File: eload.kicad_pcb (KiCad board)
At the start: 2 copper layers, 78.7 x 99.1 mm, 64 parts, among them J1 Device Power, J2 Input, J3 JST Header, J4 SWD Header, J6 JST Header, J7 Conn_02x06_Odd_Even, K1 G5Q-1, Q1 TIP122, Q2 HL 40N05, Q3 DTC043Z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

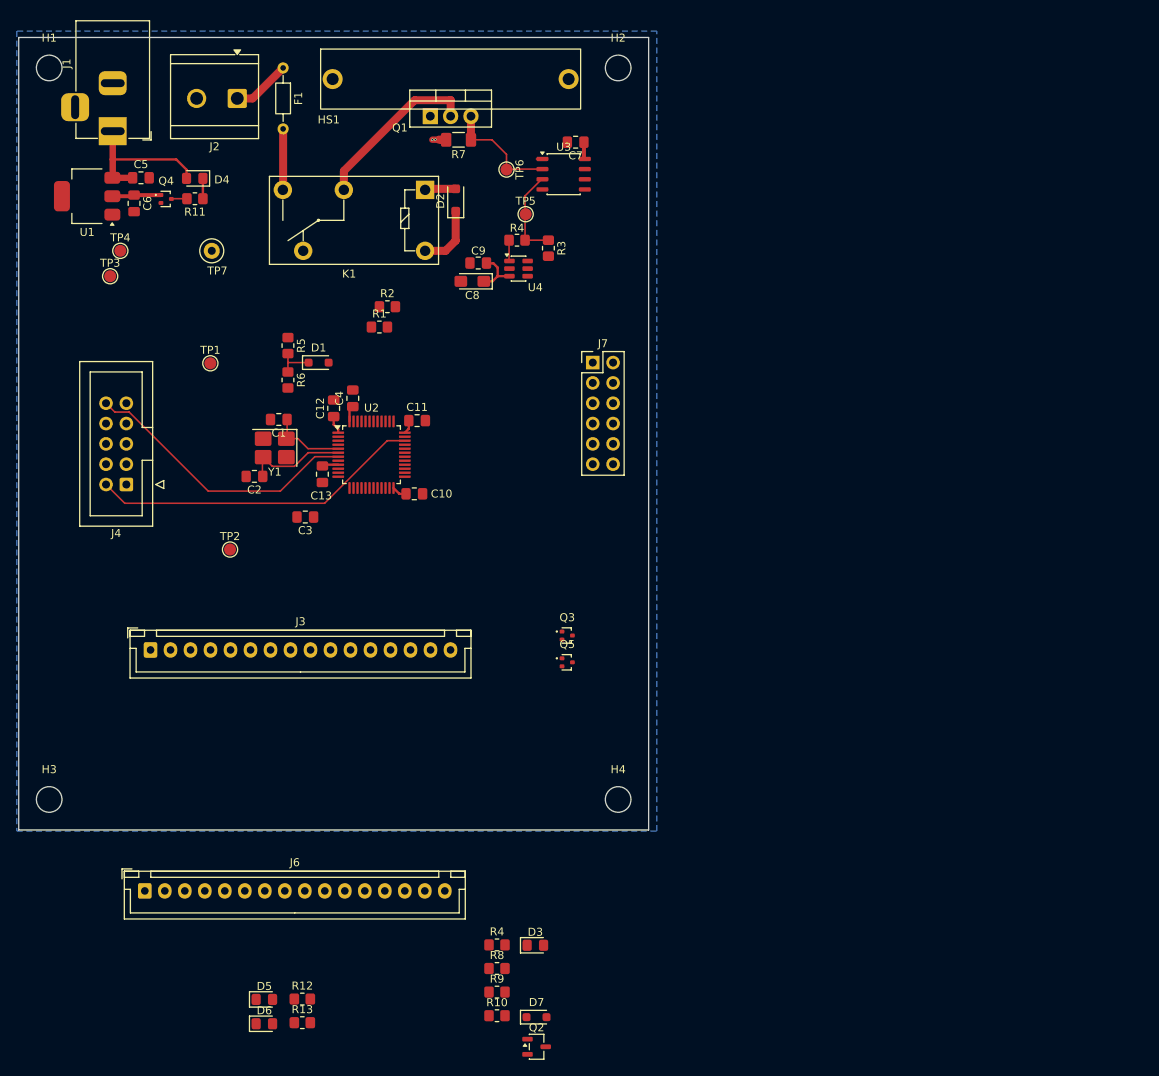
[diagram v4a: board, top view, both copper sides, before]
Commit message: PCB routing and cleanup
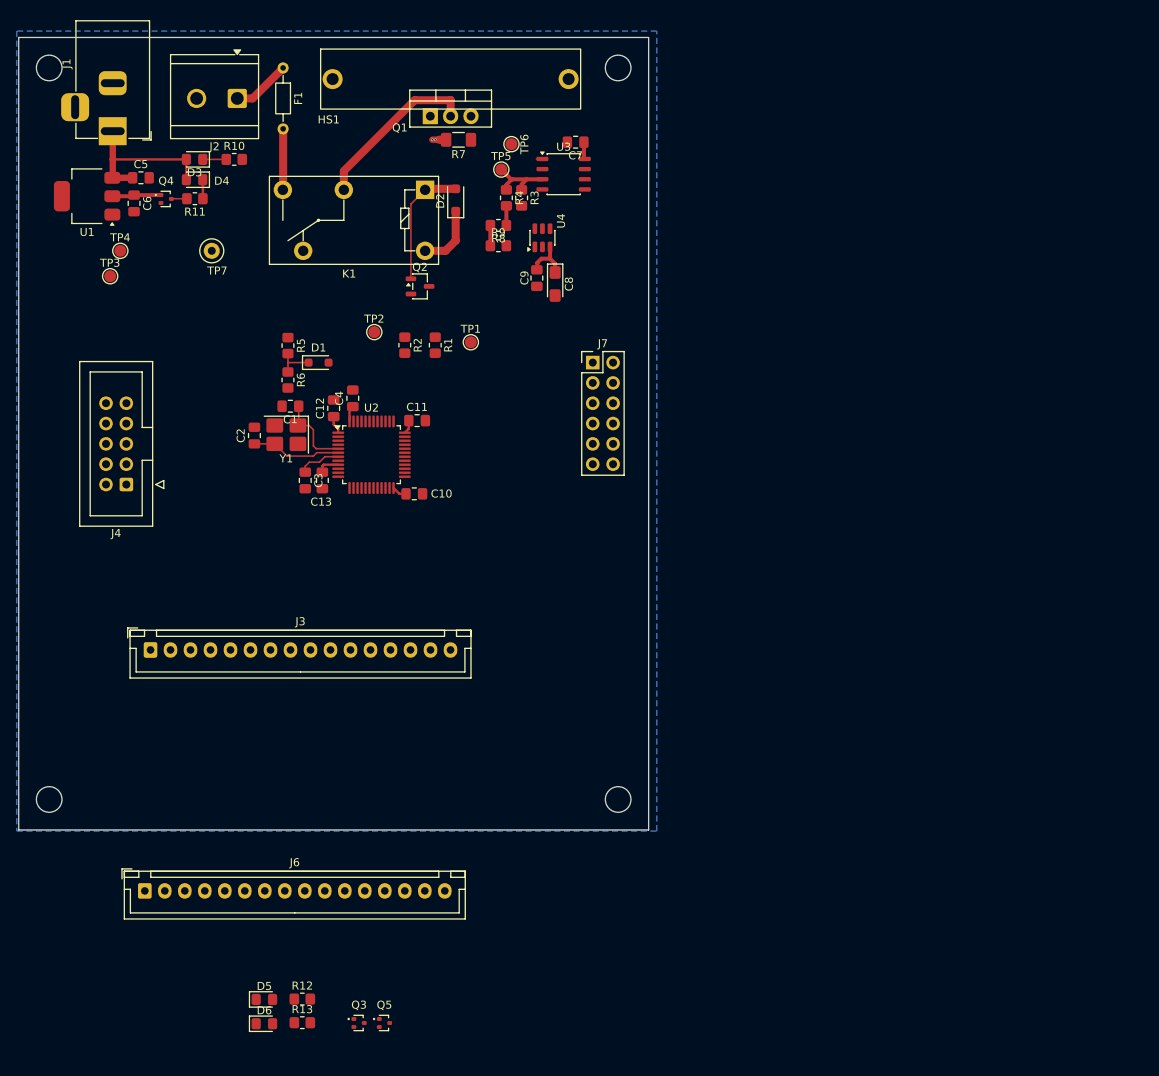
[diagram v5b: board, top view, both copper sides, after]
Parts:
- removed D7: BZT52C3V3S, Diode_SMD:D_SOD-323_HandSoldering
- removed the R4 at (77.5, 76.1)
- moved R10 112.0 mm to (42.2, 66.0)
- moved D3 107.1 mm to (37.2, 66.0), turned to 180 degrees
- moved Q2 96.2 mm to (65.4, 81.9)
- moved R4 93.4 mm to (76.2, 70.8), turned to -90 degrees
- moved R9 93.3 mm to (75.2, 76.8)
- moved R8 92.9 mm to (75.2, 74.3), turned to 180 degrees
- moved Q3 55.0 mm to (57.8, 174.0)
- moved Q5 50.5 mm to (61.0, 174.0)
- moved TP1 32.7 mm to (71.8, 88.9)
- moved TP2 32.6 mm to (59.7, 87.6)
- moved C8 10.4 mm to (82.3, 81.6), turned to -90 degrees
- moved C9 7.57 mm to (80.0, 80.9), turned to -90 degrees
- moved R1 7.34 mm to (67.3, 89.3), turned to -90 degrees
- moved R3 7.12 mm to (78.1, 70.8)
- moved TP5 6.35 mm to (75.6, 67.3)
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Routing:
- net /SWDIO: track 41.6 -> 0.00 mm
- net /~{RESET}: track 35.4 -> 5.36 mm
- net /VCC_sense: track 14.6 -> 0.00 mm
- net Net-(D2-A): track 3.88 -> 15.7 mm
- net Net-(D3-K): track 0.00 -> 2.94 mm
- net /Vctrl: track 11.5 -> 8.84 mm
- net Net-(U4-VOUT): track 2.62 -> 0.00 mm
- net Net-(R8-Pad2): track 0.00 -> 2.54 mm
- net Net-(R4-Pad2): track 0.00 -> 2.45 mm
- net /OSC2: track 13.0 -> 11.4 mm
- net +5V: track 29.4 -> 30.3 mm
- net +3.3V: track 22.2 -> 23.0 mm

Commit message: PCB routing
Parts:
- TP1: footprint TestPoint:TestPoint_Pad_D1.5mm -> TestPoint:TestPoint_Loop_D1.80mm_Drill1.0mm_Beaded
- moved R10 9.21 mm to (33.0, 67.0)
- moved C5 0.98 mm to (30.5, 69.3)
- moved C6 0.98 mm to (29.7, 72.5)
- moved D3 0.98 mm to (37.2, 67.0)
- moved D4 0.98 mm to (37.2, 69.6)
- moved Q4 0.98 mm to (33.7, 72.0)
- moved R11 0.98 mm to (37.3, 71.9)
- moved U1 0.98 mm to (23.8, 71.6)
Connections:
- D3 pad 1: Net-(D3-K) -> GND
- D3 pad 2: +5V -> Net-(D3-A)
- R10 pad 1: Net-(D3-K) -> +5V
- R10 pad 2: GND -> Net-(D3-A)
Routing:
- net Net-(D3-K): track 2.94 -> 0.00 mm
- net Net-(D3-A): track 0.00 -> 1.77 mm
- net +5V: track 30.3 -> 28.8 mm
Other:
- board text added: "3V3"
- board text added: "5V"

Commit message: Transistor updated to MOSFET
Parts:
- Q1: value TIP122 -> RFP30N06LE-VB
- moved Q1 0.32 mm to (66.7, 61.0)
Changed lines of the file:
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@@
 	(net 18 "/SWCLK")
 	(net 19 "/SWDIO")
-	(net 20 "Net-(Q1-B)")
+	(net 20 "Net-(Q1-G)")
 	(net 21 "/VCC_sense")
 	(net 22 "VCC")
@@
 		)
 	)
+	(footprint "Package_TO_SOT_THT:TO-220-3_Vertical"
+		(layer "F.Cu")
+		(at 66.69 60.96)
+		(descr "TO-220-3, Vertical, RM 2.54mm, see https://www.vishay.com/docs/66542/to-220-1.pdf, generated with kicad-footprint-generator TO_SOT_THT_generate.py")
+		(tags "TO-220-3 Vertical RM 2.54mm")
+		(property "Reference" "Q1"
+			(at 2.54 -4.1 0)
+			(layer "F.SilkS")
+			(effects
+				(font
+					(size 1 1)
+					(thickness 0.15)
+				)
+			)
+		)
+		(property "Value" "RFP30N06LE-VB"
+			(at 2.54 2.2 0)
+			(layer "F.Fab")
+			(effects
+				(font
+					(size 1 1)
+					(thickness 0.15)
+				)
+			)
+		)
+		(property "Datasheet" "https://www.lcsc.com/datasheet/C878812.pdf"
+			(at 0 0 0)
+			(layer "F.Fab")
+			(hide yes)
+			(effects
+				(font
+					(size 1.27 1.27)
+					(thickness 0.15)
+				)
+			)
+		)
+		(property "Description" "N-MOSFET transistor, gate/drain/source"
+			(at 0 0 0)
+			(layer "F.Fab")
+			(hide yes)
+			(effects
+				(font
+					(size 1.27 1.27)
+					(thickness 0.15)
+				)
+			)
+		)
+		(property "LCSC Part #" "C878812"
+			(at 0 0 0)
+			(unlocked yes)
+			(layer "F.Fab")
+			(hide yes)
+			(effects
+				(font
+					(size 1 1)
+					(thickness 0.15)
+				)
+			)
+		)
+		(sheetname "/")
+		(sheetfile "eload.kicad_sch")
+		(attr through_hole)
+		(fp_line
+			(start -2.57 -3.26)
+			(end 7.65 -3.26)
+			(stroke
+				(width 0.12)
+				(type solid)
+			)
+			(layer "F.SilkS")
+		)
+		(fp_line
+			(start -2.57 -1.88)
+			(end 7.65 -1.88)
+			(stroke
+				(width 0.12)
+				(type solid)
+			)
+			(layer "F.SilkS")
+		)
+		(fp_line
+			(start -2.57 1.36)
+			(end -2.57 -3.26)
+			(stroke
+				(width 0.12)
+				(type solid)
+			)
+			(layer "F.SilkS")
+		)
+		(fp_line
+			(start 0.69 -3.26)
+			(end 0.69 -1.88)
+			(stroke
+				(width 0.12)
+				(type solid)
+			)
+			(layer "F.SilkS")
+		)
+		(fp_line
+			(start 4.39 -3.26)
+			(end 4.39 -1.88)
+			(stroke
+				(width 0.12)
+				(type solid)
+			)
+			(layer "F.SilkS")
+		)
+		(fp_line
+			(start 7.65 -3.26)
+			(end 7.65 1.36)
+			(stroke
+				(width 0.12)
+				(type solid)
+			)
+			(layer "F.SilkS")
+		)
+		(fp_line
+			(start 7.65 1.36)
+			(end -2.57 1.36)
+			(stroke
+				(width 0.12)
+				(type solid)
+			)
+			(layer "F.SilkS")
+		)
+		(fp_rect
+			(start -2.71 -3.4)
+			(end 7.79 1.5)
+			(stroke
+				(width 0.05)
+				(type solid)
+			)
+			(fill no)
+			(layer "F.CrtYd")
+		)
+		(fp_line
+			(start -2.46 -1.88)
+			(end 7.54 -1.88)
+			(stroke
+				(width 0.1)
+				(type solid)
+			)
+			(layer "F.Fab")
+		)
+		(fp_line
+			(start 0.69 -3.15)
+			(end 0.69 -1.88)
+			(stroke
+				(width 0.1)
+				(type solid)
+			)
+			(layer "F.Fab")
+		)
+		(fp_line
+			(start 4.39 -3.15)
+			(end 4.39 -1.88)
+			(stroke
+				(width 0.1)
+				(type solid)
+			)
+			(layer "F.Fab")
+		)
+		(fp_rect
+			(start -2.46 -3.15)
+			(end 7.54 1.25)
+			(stroke
+				(width 0.1)
+				(type solid)
+			)
+			(fill no)
+			(layer "F.Fab")
+		)
+		(fp_text user "${REFERENCE}"
+			(at 2.54 -0.95 0)
+			(layer "F.Fab")
+			(effects
+				(font
+					(size 1 1)
+					(thickness 0.15)
+				)
+			)
+		)
+		(pad "1" thru_hole rect
+			(at 0 0)
+			(size 1.905 2)
+			(drill 1.1)
+			(layers "*.Cu" "*.Mask")
+			(remove_unused_layers no)
+			(net 20 "Net-(Q1-G)")
+			(pinfunction "G")
+			(pintype "input")
+		)
+		(pad "2" thru_hole oval
+			(at 2.54 0)
+			(size 1.905 2)
+			(drill 1.1)
+			(layers "*.Cu" "*.Mask")
+			(remove_unused_layers no)
+			(net 22 "VCC")
+			(pinfunction "D")
+			(pintype "passive")
+		)
+		(pad "3" thru_hole oval
+			(at 5.08 0)
+			(size 1.905 2)
+			(drill 1.1)
+			(layers "*.Cu" "*.Mask")
+			(remove_unused_layers no)
+			(net 21 "/VCC_sense")
+			(pinfunction "S")
+			(pintype "passive")
+		)
+		(embedded_fonts no)
+		(model "${KICAD9_3DMODEL_DIR}/Package_TO_SOT_THT.3dshapes/TO-220-3_Vertical.step"
+			(offset
+				(xyz 0 0 2)
+			)
+			(scale
+				(xyz 1 1 1)
+			)
+			(rotate
+				(xyz -0 -0 -0)
+			)
+		)
+	)
 	(footprint "Capacitor_SMD:C_0805_2012Metric_Pad1.18x1.45mm_HandSolder"
 		(layer "F.Cu")
@@
 		)
 	)
-	(footprint "Package_TO_SOT_THT:TO-220-3_Vertical"
-		(locked yes)
-		(layer "F.Cu")
-		(at 66.69 60.64)
-		(descr "TO-220-3, Vertical, RM 2.54mm, see https://www.vishay.com/docs/66542/to-220-1.pdf, generated with kicad-footprint-generator TO_SOT_THT_generate.py")
-		(tags "TO-220-3 Vertical RM 2.54mm")
-		(property "Reference" "Q1"
-			(at -3.81 1.446 0)
-			(layer "F.SilkS")
-			(effects
-				(font
-					(size 1 1)
-					(thickness 0.15)
-				)
-			)
-		)
-		(property "Value" "TIP122"
-			(at 2.54 2.2 0)
-			(layer "F.Fab")
-			(effects
-				(font
-					(size 1 1)
-					(thickness 0.15)
-				)
-			)
-		)
-		(property "Datasheet" "https://www.onsemi.com/pub/Collateral/TIP120-D.PDF"
-			(at 0 0 0)
-			(layer "F.Fab")
-			(hide yes)
-			(effects
-				(font
-					(size 1.27 1.27)
-					(thickness 0.15)
-				)
-			)
-		)
-		(property "Description" "5A Ic, 100V Vce, Silicon Darlington Power NPN Transistor, TO-220"
-			(at 0 0 0)
-			(layer "F.Fab")
-			(hide yes)
-			(effects
-				(font
-					(size 1.27 1.27)
-					(thickness 0.15)
-				)
-			)
-		)
-		(property "LCSC Part #" "C16283"
-			(at 0 0 0)
-			(unlocked yes)
-			(layer "F.Fab")
-			(hide yes)
-			(effects
-				(font
-					(size 1 1)
-					(thickness 0.15)
-				)
-			)
-		)
-		(property ki_fp_filters "TO?220*")
-		(sheetname "/")
-		(sheetfile "eload.kicad_sch")
-		(attr through_hole)
-		(fp_line
-			(start -2.57 -3.26)
-			(end 7.65 -3.26)
-			(stroke
-				(width 0.12)
-				(type solid)
-			)
-			(layer "F.SilkS")
-		)
-		(fp_line
-			(start -2.57 -1.88)
-			(end 7.65 -1.88)
-			(stroke
-				(width 0.12)
-				(type solid)
-			)
-			(layer "F.SilkS")
-		)
-		(fp_line
-			(start -2.57 1.36)
-			(end -2.57 -3.26)
-			(stroke
-				(width 0.12)
-				(type solid)
-			)
-			(layer "F.SilkS")
-		)
-		(fp_line
-			(start 0.69 -3.26)
-			(end 0.69 -1.88)
-			(stroke
-				(width 0.12)
-				(type solid)
-			)
-			(layer "F.SilkS")
-		)
-		(fp_line
-			(start 4.39 -3.26)
-			(end 4.39 -1.88)
-			(stroke
-				(width 0.12)
-				(type solid)
-			)
-			(layer "F.SilkS")
-		)
-		(fp_line
-			(start 7.65 -3.26)
-			(end 7.65 1.36)
-			(stroke
-				(width 0.12)
-				(type solid)
-			)
-			(layer "F.SilkS")
-		)
-		(fp_line
-			(start 7.65 1.36)
-			(end -2.57 1.36)
-			(stroke
-				(width 0.12)
-				(type solid)
-			)
-			(layer "F.SilkS")
-		)
-		(fp_rect
-			(start -2.71 -3.4)
-			(end 7.79 1.5)
-			(stroke
-				(width 0.05)
-				(type solid)
-			)
-			(fill no)
-			(layer "F.CrtYd")
-		)
-		(fp_line
-			(start -2.46 -1.88)
-			(end 7.54 -1.88)
-			(stroke
-				(width 0.1)
-				(type solid)
-			)
-			(layer "F.Fab")
-		)
-		(fp_line
-			(start 0.69 -3.15)
-			(end 0.69 -1.88)
-			(stroke
-				(width 0.1)
-				(type solid)
-			)
-			(layer "F.Fab")
-		)
-		(fp_line
-			(start 4.39 -3.15)
-			(end 4.39 -1.88)
-			(stroke
-				(width 0.1)
-				(type solid)
-			)
-			(layer "F.Fab")
-		)
-		(fp_rect
-			(start -2.46 -3.15)
-			(end 7.54 1.25)
-			(stroke
-				(width 0.1)
-				(type solid)
-			)
-			(fill no)
-			(layer "F.Fab")
-		)
-		(fp_text user "${REFERENCE}"
-			(at 2.54 -0.95 0)
-			(layer "F.Fab")
-			(effects
-				(font
-					(size 1 1)
-					(thickness 0.15)
-				)
-			)
-		)
-		(pad "1" thru_hole rect
-			(at 0 0)
-			(size 1.905 2)
-			(drill 1.1)
-			(layers "*.Cu" "*.Mask")
-			(remove_unused_layers no)
-			(net 20 "Net-(Q1-B)")
-			(pinfunction "B")
-			(pintype "input")
-		)
-		(pad "2" thru_hole oval
-			(at 2.54 0)
-			(size 1.905 2)
-			(drill 1.1)
-			(layers "*.Cu" "*.Mask")
-			(remove_unused_layers no)
-			(net 22 "VCC")
-			(pinfunction "C")
-			(pintype "passive")
-		)
-		(pad "3" thru_hole oval
-			(at 5.08 0)
-			(size 1.905 2)
-			(drill 1.1)
-			(layers "*.Cu" "*.Mask")
-			(remove_unused_layers no)
-			(net 21 "/VCC_sense")
-			(pinfunction "E")
-			(pintype "passive")
-		)
-		(embedded_fonts no)
-		(model "${KICAD9_3DMODEL_DIR}/Package_TO_SOT_THT.3dshapes/TO-220-3_Vertical.step"
-			(offset
-				(xyz 0 0 2)
-			)
-			(scale
-				(xyz 1 1 1)
-			)
-			(rotate
-				(xyz -0 -0 -0)
-			)
-		)
-	)
 	(footprint "Capacitor_SMD:C_0805_2012Metric_Pad1.18x1.45mm_HandSolder"
 		(layer "F.Cu")
@@
 			(layers "F.Cu" "F.Mask" "F.Paste")
 			(roundrect_rratio 0.25)
-			(net 20 "Net-(Q1-B)")
+			(net 20 "Net-(Q1-G)")
 			(pintype "output")
 		)

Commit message: Update digital transistor to more solderable by hand
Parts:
- Q3, Q4, Q5: value DTC043Z -> DTC043ZUBTL; footprint Package_TO_SOT_SMD:SOT-416 -> Package_TO_SOT_SMD:SOT-323_SC-70
- moved TP4 4.93 mm to (30.7, 81.5)
- moved TP3 3.35 mm to (24.6, 83.3)
- moved Q4 0.41 mm to (33.3, 72.1)
- moved R11 0.20 mm to (37.3, 72.1)
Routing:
- net +3.3V: track 23.0 -> 22.2 mm
